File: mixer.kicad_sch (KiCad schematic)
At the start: 49 parts, among them T1 RF_BALUN, T2 RF_BALUN, U4 RFFC5072, U5 FM8625H, U6 FM8625H

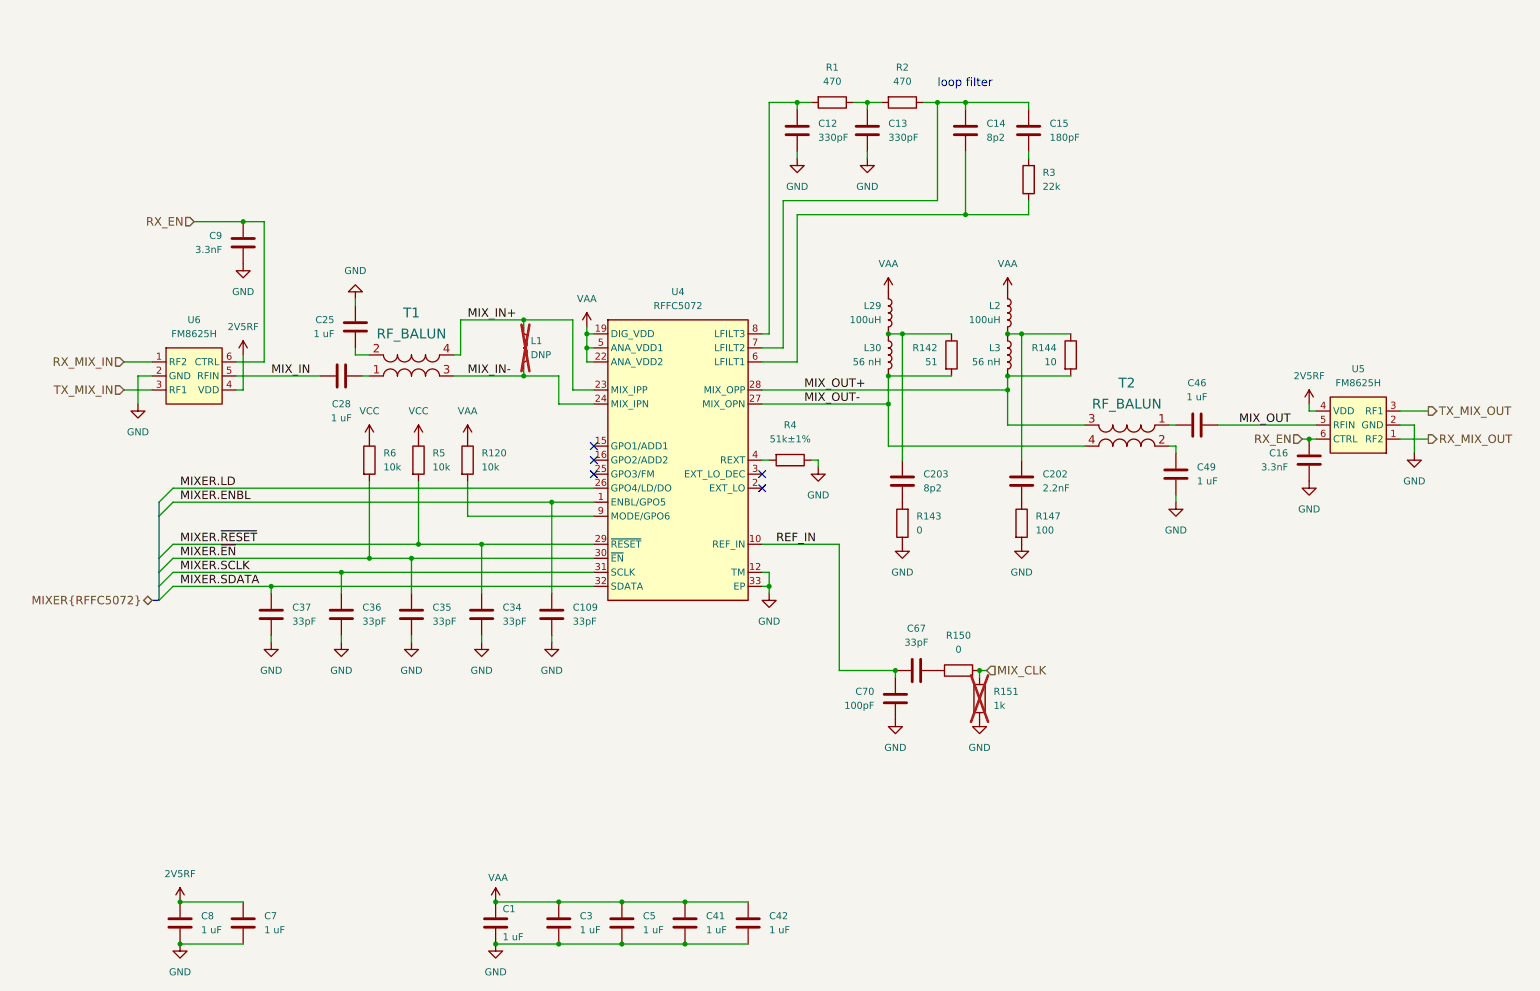
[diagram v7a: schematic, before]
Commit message: Replace mixer compensation amps with single BGB741
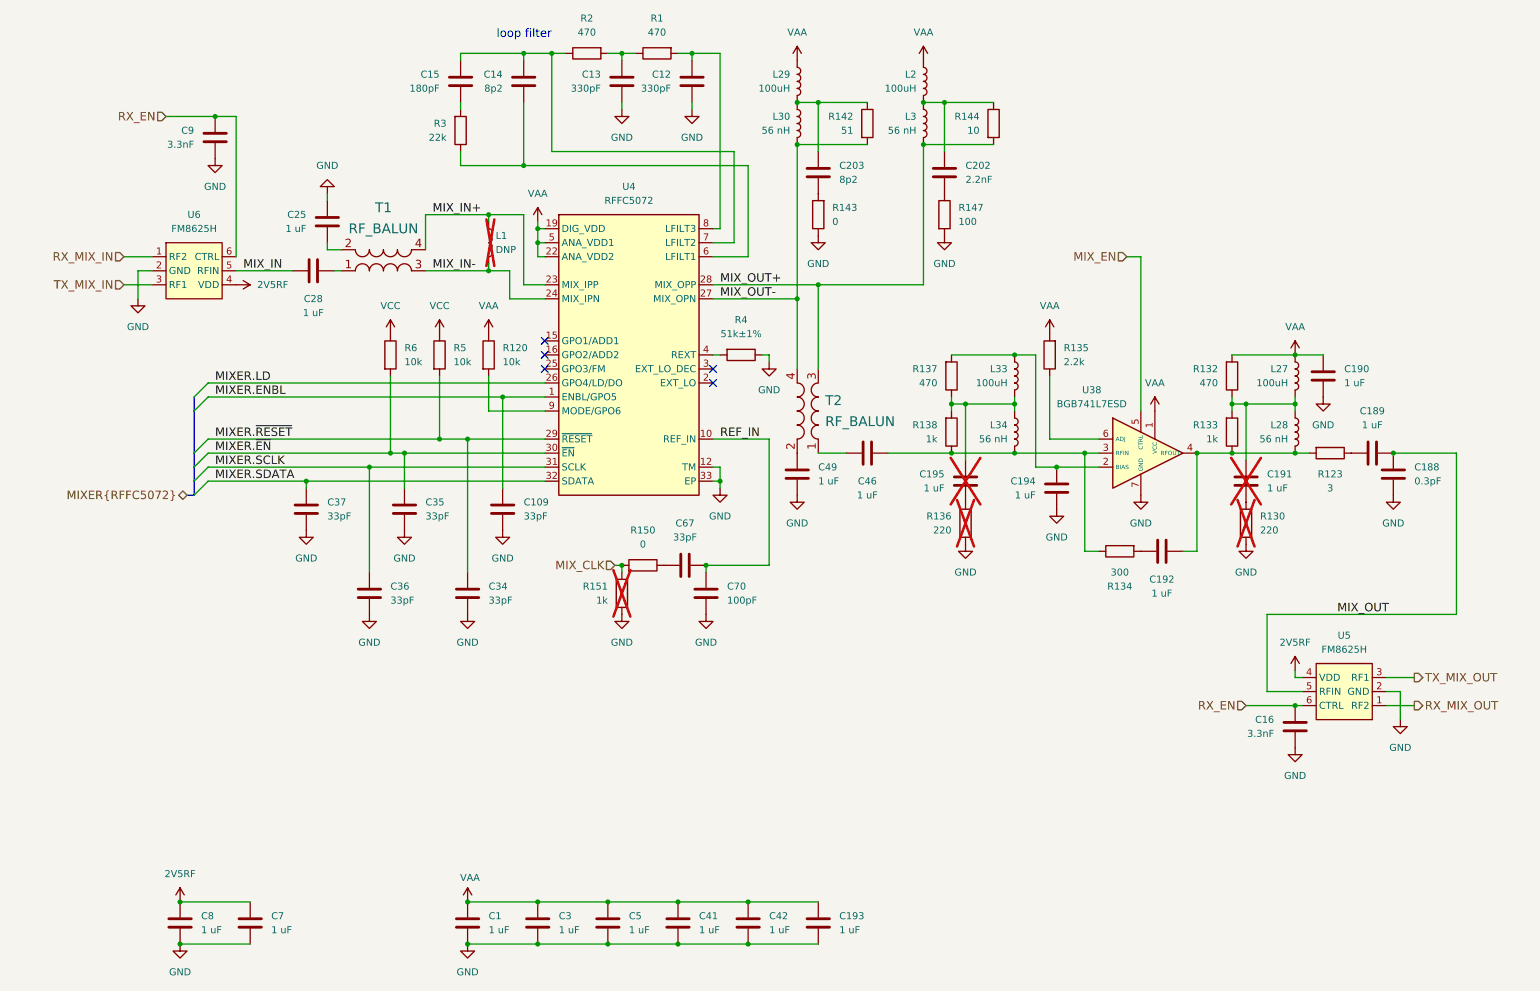
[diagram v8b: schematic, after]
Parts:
- added C188: 0.3pF, Capacitor_SMD:C_0201_0603Metric, symbol Device:C
- added C189, C190, C191, C192, C193, C194, C195: 1 uF, Capacitor_SMD:C_0201_0603Metric, symbol Device:C
- added L27, L33: 100uH, praline:L_TDK_MLZ2012_h1.25mm, symbol Device:L
- added L28, L34: 56 nH, Inductor_SMD:L_0201_0603Metric, symbol Device:L
- added R123: 3, Resistor_SMD:R_0201_0603Metric, symbol Device:R
- added R130, R136: 220, Resistor_SMD:R_0201_0603Metric, symbol Device:R
- added R132, R137: 470, Resistor_SMD:R_0201_0603Metric, symbol Device:R
- added R133, R138: 1k, Resistor_SMD:R_0201_0603Metric, symbol Device:R
- added R134: 300, Resistor_SMD:R_0201_0603Metric, symbol Device:R
- added R135: 2.2k, Resistor_SMD:R_0201_0603Metric, symbol Device:R
- added U38: BGB741L7ESD, praline:TSLP-7-1, symbol praline:BGB741L7ESD
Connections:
- net GND: now also C188.2, C190.2, C193.2, C194.2, R130.1, R136.1, U38.7 (GND)
- net MIX_OUT: now also C188.1, C189.1; no longer C46.1
- net VAA: now also C190.1, C193.1, L27.1, R132.2, R135.2, U38.1 (VCC)
- new net: C192.1, L28.2, R123.2, R133.1, U38.4 (RFOUT)
- new net: C192.2, R134.2
- new net: C189.2, R123.1
- new net: C191.1, L27.2, L28.1, R132.1, R133.2
- new net: C191.2, R130.2
- new net: C194.1, L33.1, R137.2, U38.2 (BIAS)
- new net: C46.1, L34.2, R134.1, R138.1, U38.3 (RFIN)
- new net: R135.1, U38.6 (ADJ)
- new net: C195.1, L33.2, L34.1, R137.1, R138.2
- new net: C195.2, R136.2
- new net MIX_EN: U38.5 (CTRL)
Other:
- moved on the sheet: C1, C109, C12, C13, C14, C15, C16, C202, C203, C25, C28, C3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
